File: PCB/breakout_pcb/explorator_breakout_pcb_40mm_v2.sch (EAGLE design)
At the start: 38 parts, among them P1 B10B-PH-K, U1 SHTC3, U2 VEML6030-GS15

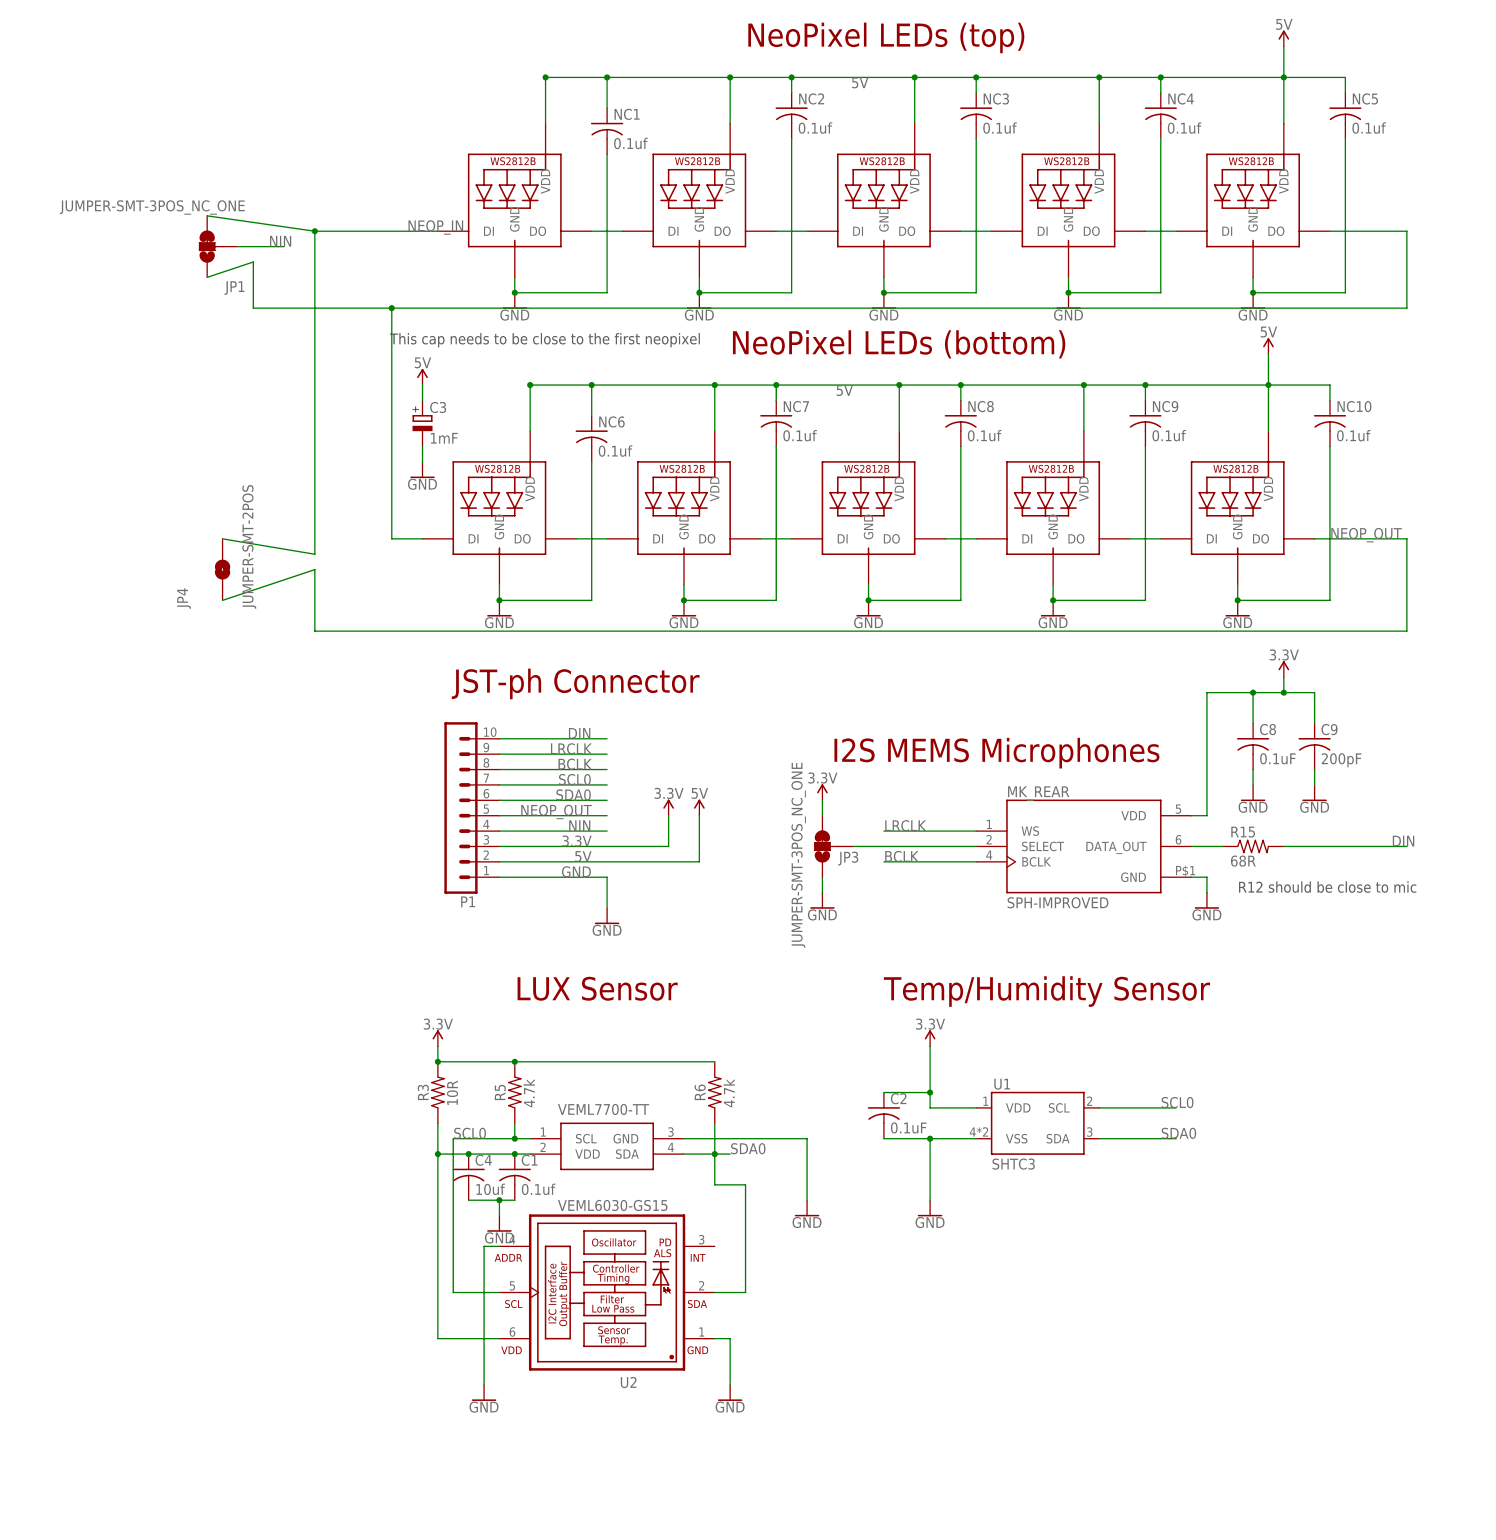
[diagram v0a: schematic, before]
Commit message: updated the breakout_pcb folder to only include the most recent PCB revision, added a README for the board, updated the parts_list, and generated gerbers
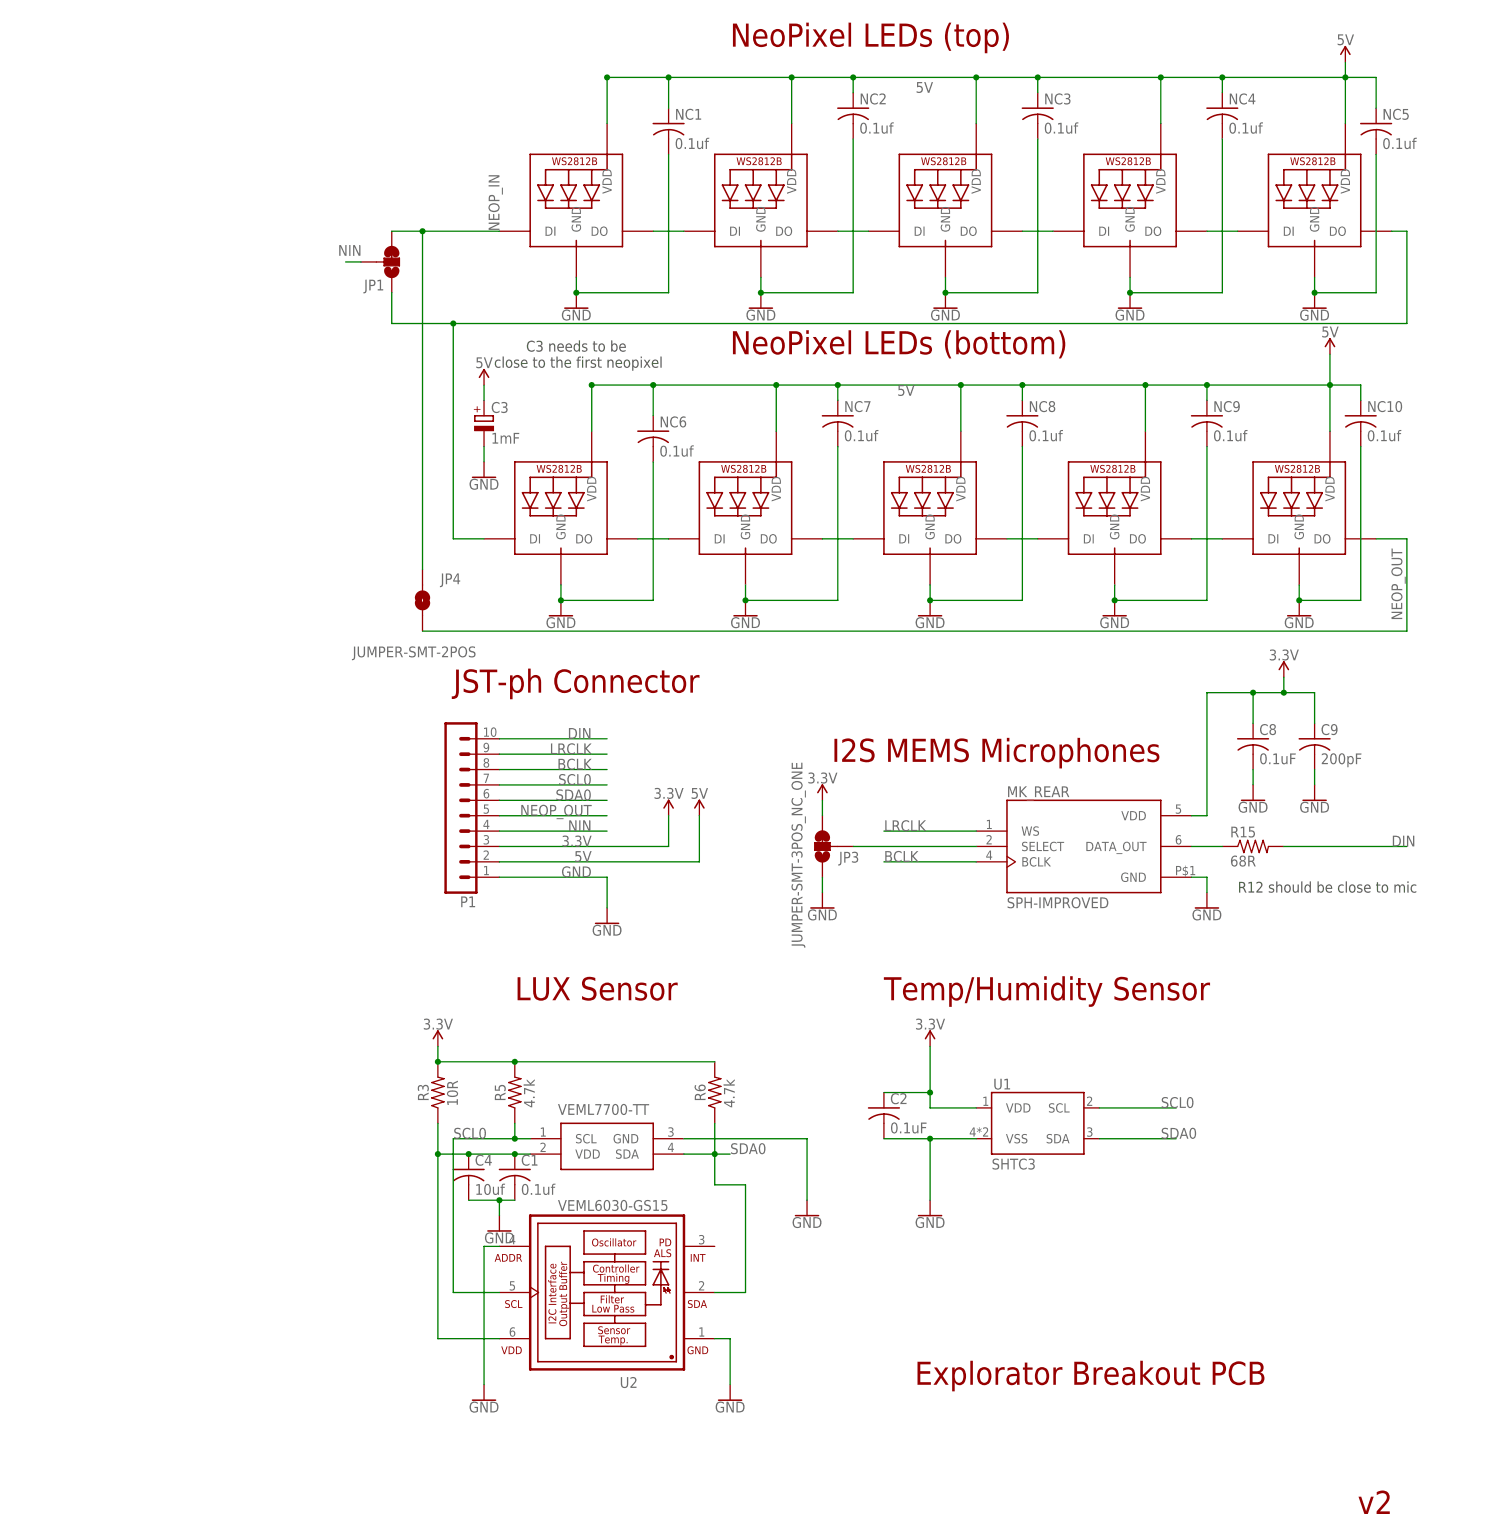
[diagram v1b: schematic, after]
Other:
- note added: "C3 needs to be close to the first neopixel"
- note added: "Explorator Breakout PCB"
- note added: "v2"
- note removed: "This cap needs to be close to the first neopixel"
- moved on the sheet: C3, JP1, JP4, NC1, NC10, NC2, NC3, NC4, NC5, NC6, NC7, NC8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
